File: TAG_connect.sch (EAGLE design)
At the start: 4 parts, among them J2 RJ11-6PTH

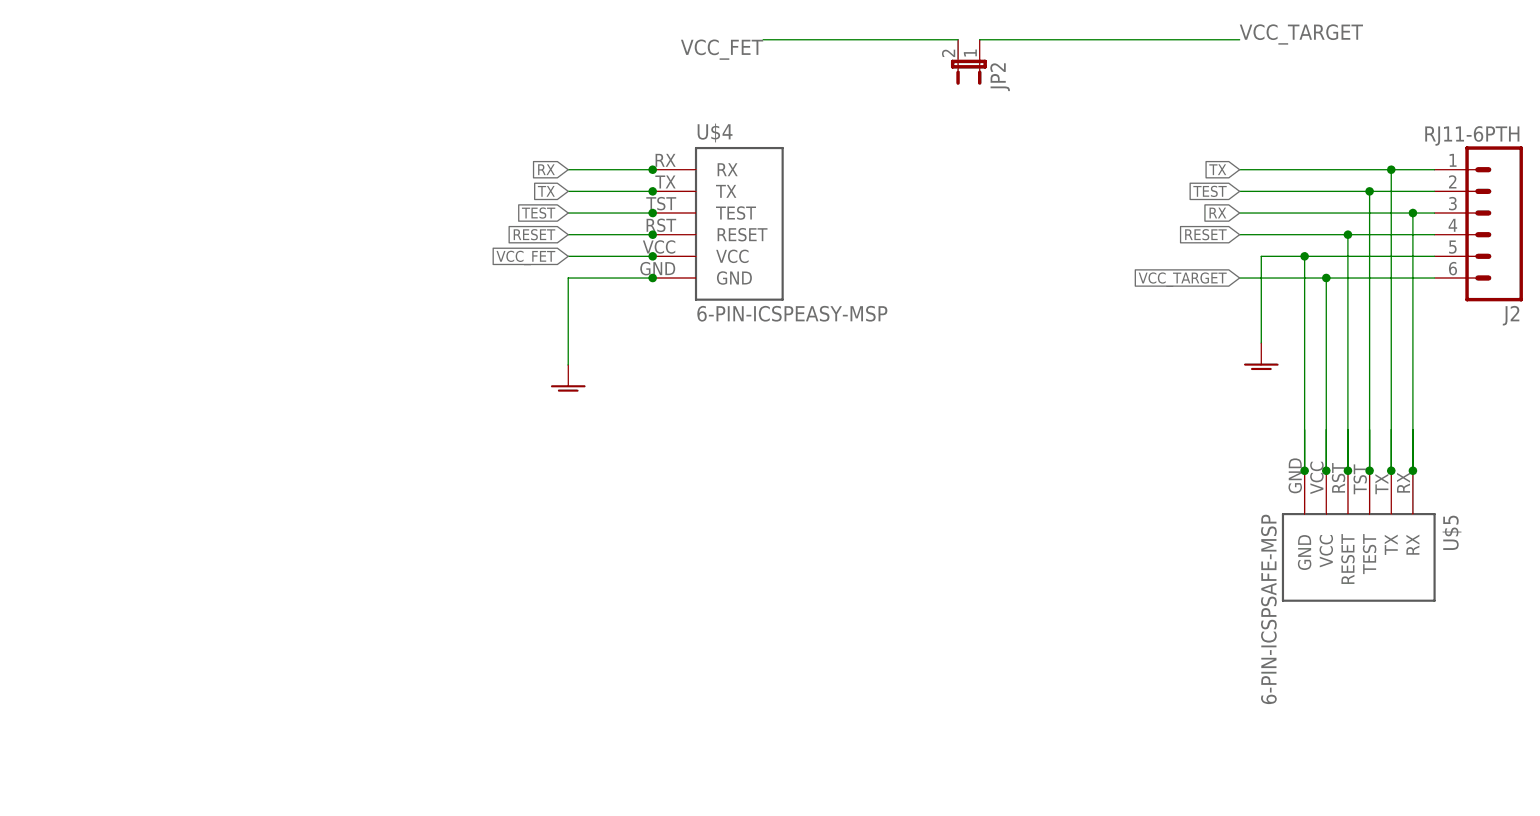
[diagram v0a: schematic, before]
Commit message: new board, new pinout
Changed the pinout on the tag-connect cable to match new work
Added new SAFE-MSP adaptor board that uses a symmetric 2x10 .015" header
for programming.
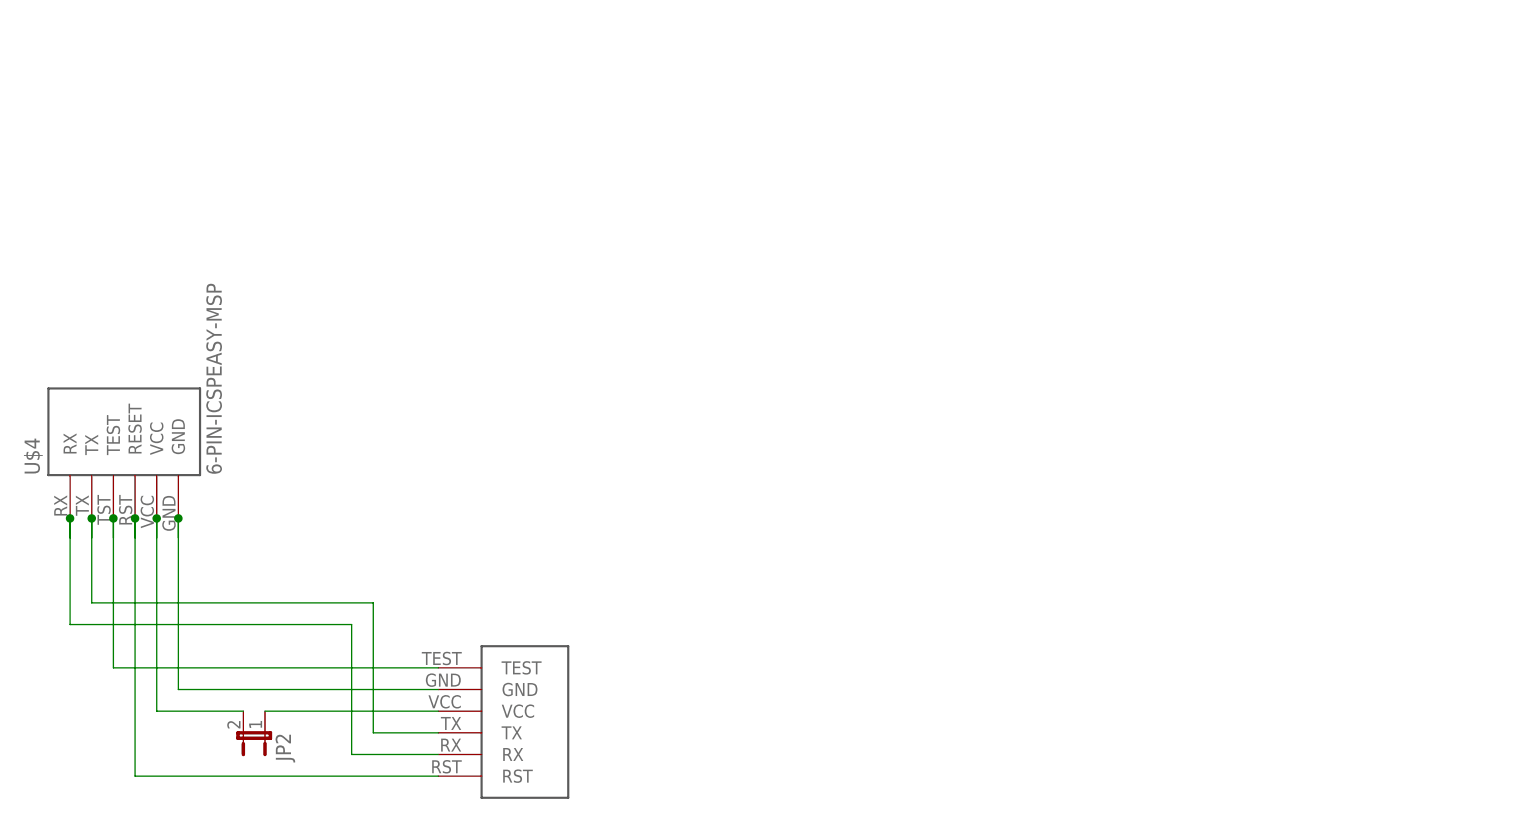
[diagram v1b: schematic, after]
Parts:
- removed J2: RJ11-6PTH, SparkFun-Connectors:RJ11-6PTH
- removed U$5: 6-PIN-ICSPSAFE-MSP, LaunchFET:6-PIN-ICSPSAFE-MSP
- added U$1: RJ-45SMD, LaunchFET:RJ-45SMD
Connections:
- removed net RESET: J2.4, U$4.RESET, U$5.RESET
- new net RST: U$1.RST, U$4.RESET
- net GND: now also U$1.GND; no longer J2.5, U$5.GND
- net RX: now also U$1.RX; no longer J2.3, U$5.RX
- net TEST: now also U$1.TEST; no longer J2.2, U$5.TEST
- net TX: now also U$1.TX; no longer J2.1, U$5.TX
- net VCC_TARGET: now also U$1.VCC; no longer J2.6, U$5.VCC
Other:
- moved on the sheet: JP2, U$4
